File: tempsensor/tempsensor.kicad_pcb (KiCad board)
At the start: 2 copper layers, 40 x 40 mm, 36 parts, among them J1 USB_B_Micro, Q4 BSS806N, Q5 BC817, SW1 PW_OFF, SW2 PW_OFF, SW3 PW_ON, U3 24C16, U4 MCP73831-2-OT, U5 MCP9844

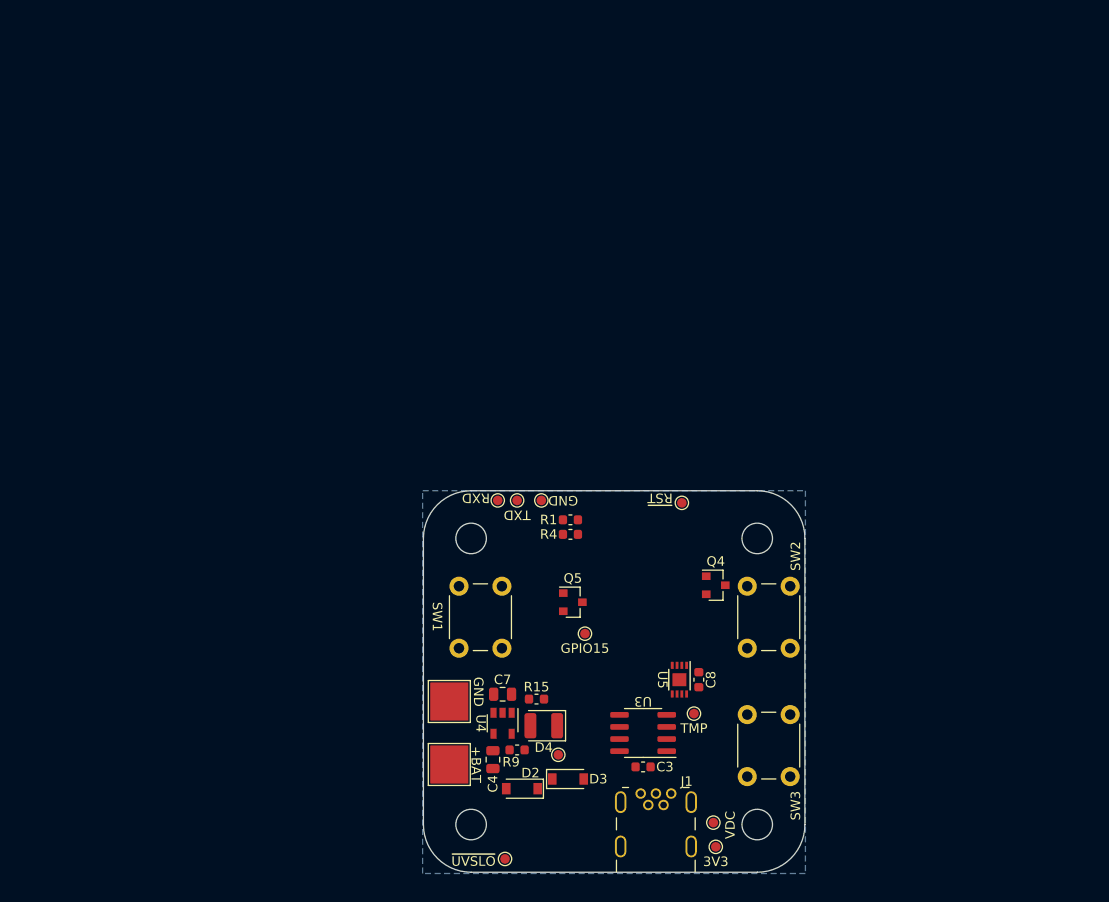
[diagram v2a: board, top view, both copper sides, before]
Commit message: Added footprints to tempsensor.
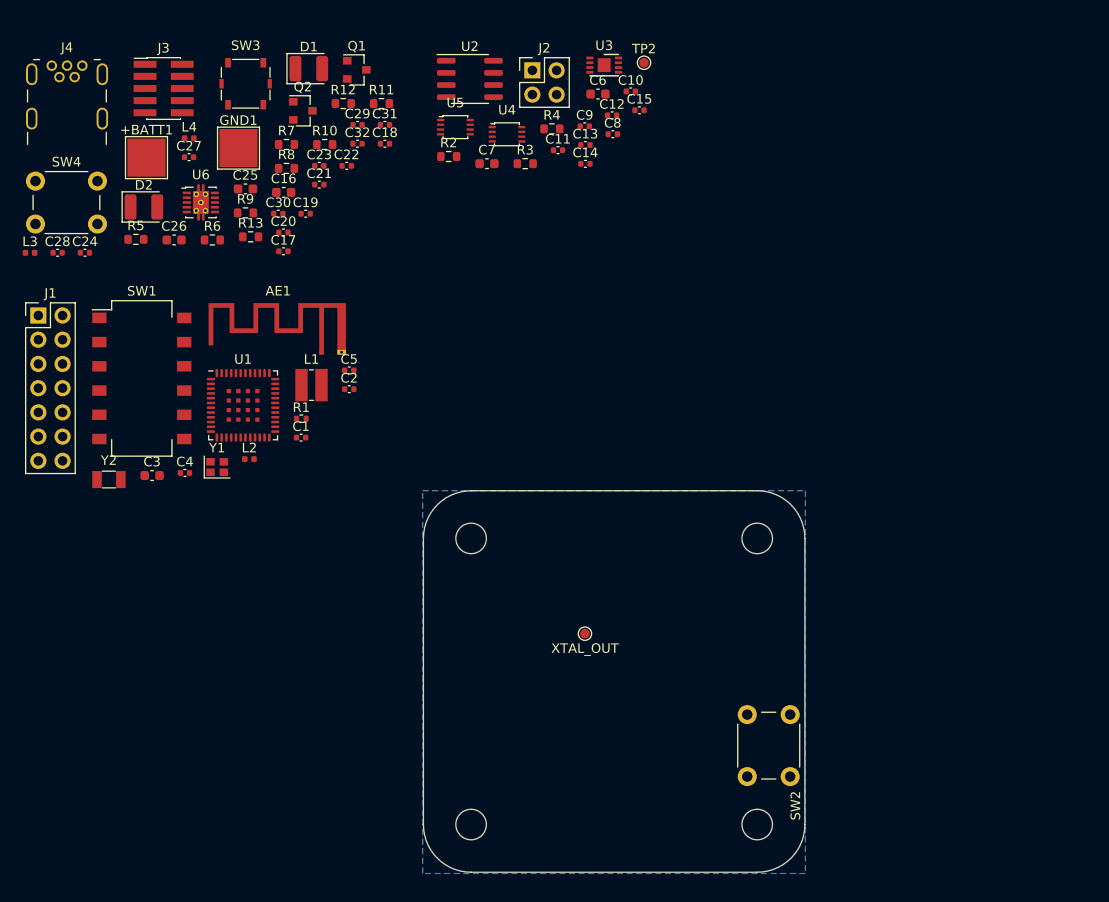
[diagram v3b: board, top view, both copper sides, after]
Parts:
- removed D3: SL03, Diode_SMD:D_SOD-123
- removed D4: LED, LED_SMD:LED_1210_3225Metric
- removed Q4: BSS806N, Package_TO_SOT_SMD:SOT-23
- removed Q5: BC817, Package_TO_SOT_SMD:SOT-23
- removed R15: 470, Resistor_SMD:R_0603_1608Metric
- removed the SW2 at (211.8, 85.1)
- removed TP12: 3V3, TestPoint:TestPoint_Pad_D1.0mm
- removed TP13: ~UVSLO, TestPoint:TestPoint_Pad_D1.0mm
- removed TP14: VDC, TestPoint:TestPoint_Pad_D1.0mm
- removed TP16: TMP, TestPoint:TestPoint_Pad_D1.0mm
- removed TP3: VBUS, TestPoint:TestPoint_Pad_D1.0mm
- removed TP4: GND, TestPoint:TestPoint_Pad_D1.0mm
- removed TP5: RXD, TestPoint:TestPoint_Pad_D1.0mm
- removed TP6: TXD, TestPoint:TestPoint_Pad_D1.0mm
- removed TP9: ~RST, TestPoint:TestPoint_Pad_D1.0mm
- added AE1: Antenna_Shield, RF_Antenna:Texas_SWRA117D_2.4GHz_Left, F.Cu at (167.2, 54.1)
- added C1: 10p, Capacitor_SMD:C_0402_1005Metric, F.Cu at (165.1, 63.0)
- added C10: 100n, Capacitor_SMD:C_0402_1005Metric, F.Cu at (199.6, 26.7)
- added C11: 1u, Capacitor_SMD:C_0402_1005Metric, F.Cu at (192.0, 32.9)
- added C12: 1u, Capacitor_SMD:C_0402_1005Metric, F.Cu at (197.7, 29.2)
- added C13: 100n, Capacitor_SMD:C_0402_1005Metric, F.Cu at (194.9, 32.3)
- added C14: 100n, Capacitor_SMD:C_0402_1005Metric, F.Cu at (194.9, 34.3)
- added C15: 1u, Capacitor_SMD:C_0402_1005Metric, F.Cu at (200.5, 28.7)
- added C16: 10u, Capacitor_SMD:C_0603_1608Metric, F.Cu at (163.2, 37.3)
- added C17: 1u, Capacitor_SMD:C_0402_1005Metric, F.Cu at (163.2, 43.5)
- added C18: 1u, Capacitor_SMD:C_0402_1005Metric, F.Cu at (173.8, 32.2)
- added C19: 100n, Capacitor_SMD:C_0402_1005Metric, F.Cu at (165.5, 39.5)
- added C2: 100n, Capacitor_SMD:C_0402_1005Metric, F.Cu at (170.1, 57.9)
- added C20: 100n, Capacitor_SMD:C_0402_1005Metric, F.Cu at (163.2, 41.5)
- added C21: 10n, Capacitor_SMD:C_0402_1005Metric, F.Cu at (167.0, 36.5)
- added C22: 10n, Capacitor_SMD:C_0402_1005Metric, F.Cu at (169.8, 34.5)
- added C23: 1u, Capacitor_SMD:C_0402_1005Metric, F.Cu at (167.0, 34.5)
- added C24: 100n, Capacitor_SMD:C_0402_1005Metric, F.Cu at (142.4, 43.6)
- added C25: 1u, Capacitor_SMD:C_0603_1608Metric, F.Cu at (159.2, 36.9)
- added C26: 10u, Capacitor_SMD:C_0603_1608Metric, F.Cu at (151.7, 42.3)
- added C27: 1u, Capacitor_SMD:C_0402_1005Metric, F.Cu at (153.3, 33.6)
- added C28: 1u, Capacitor_SMD:C_0402_1005Metric, F.Cu at (139.5, 43.6)
- added C29: 100n, Capacitor_SMD:C_0402_1005Metric, F.Cu at (171.0, 30.2)
- added C30: 12p, Capacitor_SMD:C_0402_1005Metric, F.Cu at (162.7, 39.5)
- added C31: 12p, Capacitor_SMD:C_0402_1005Metric, F.Cu at (173.8, 30.2)
- added C32: 100n, Capacitor_SMD:C_0402_1005Metric, F.Cu at (171.0, 32.2)
- added C5: 0,7p, Capacitor_SMD:C_0402_1005Metric, F.Cu at (170.1, 56.0)
- added C6: 100n, Capacitor_SMD:C_0603_1608Metric, F.Cu at (196.2, 27.0)
- added C9: 100n, Capacitor_SMD:C_0402_1005Metric, F.Cu at (194.8, 30.4)
- added D1: LED, LED_SMD:LED_1210_3225Metric, F.Cu at (165.9, 24.3)
- added J2: Conn_01x04, Connector_PinHeader_2.54mm:PinHeader_2x02_P2.54mm_Vertical, F.Cu at (189.3, 24.5)
- added J3: Conn_ARM_JTAG_SWD_10, Connector_PinHeader_1.27mm:PinHeader_2x05_P1.27mm_Vertical_SMD, F.Cu at (150.6, 26.4)
- added J4: USB_B_Micro, myfootprints:USB-Mini-B_Wuerth_651005136521_Horizontal, F.Cu at (138.9, 24.0)
- added L1: 10u, Inductor_SMD:L_Wuerth_MAPI-3012, F.Cu at (166.1, 57.5)
- added L2: 5,6n, Inductor_SMD:L_0402_1005Metric, F.Cu at (159.6, 65.3)
- added L3: 100n, Inductor_SMD:L_0402_1005Metric, F.Cu at (136.6, 43.6)
- added L4: 100n, Inductor_SMD:L_0402_1005Metric, F.Cu at (153.3, 31.6)
- added Q1: BSS806N, Package_TO_SOT_SMD:SOT-23, F.Cu at (170.9, 24.5)
- added Q2: BSS806N, Package_TO_SOT_SMD:SOT-23, F.Cu at (165.2, 28.7)
- added R10: R, Resistor_SMD:R_0603_1608Metric, F.Cu at (167.5, 32.3)
- added R11: R, Resistor_SMD:R_0603_1608Metric, F.Cu at (173.5, 28.0)
- added R12: R, Resistor_SMD:R_0603_1608Metric, F.Cu at (169.5, 28.0)
- added R13: R, Resistor_SMD:R_0603_1608Metric, F.Cu at (159.8, 42.0)
- added R2: 2K2, Resistor_SMD:R_0603_1608Metric, F.Cu at (180.5, 33.5)
- added R3: 2K2, Resistor_SMD:R_0603_1608Metric, F.Cu at (188.6, 34.3)
- added R5: R, Resistor_SMD:R_0603_1608Metric, F.Cu at (147.7, 42.2)
- added R6: R, Resistor_SMD:R_0603_1608Metric, F.Cu at (155.8, 42.3)
- added R7: R, Resistor_SMD:R_0603_1608Metric, F.Cu at (163.5, 32.3)
- added R8: R, Resistor_SMD:R_0603_1608Metric, F.Cu at (163.5, 34.8)
- added SW3: ~RST, Button_Switch_SMD:SW_SPST_Panasonic_EVQPL_3PL_5PL_PT_A08, F.Cu at (159.2, 25.9)
- added SW4: ~INT, Button_Switch_THT:SW_PUSH_6mm_H5mm, F.Cu at (137.2, 36.1)
- added TP2: ~TMP_INT, TestPoint:TestPoint_Pad_D1.0mm, F.Cu at (201.0, 23.7)
- added U1: MKW41Z512VHT, Package_DFN_QFN:NXP_LQFN-48-1EP_7x7mm_P0.5mm_EP3.5x3.5mm_16xMask0.45x0.45, F.Cu at (159.0, 59.6)
- added U2: 24C16, Package_SO:SOIC-8_3.9x4.9mm_P1.27mm, F.Cu at (182.8, 25.4)
- added U6: BQ24012, Package_SON:VSON-10-1EP_3x3mm_P0.5mm_EP1.65x2.4mm_ThermalVias, F.Cu at (154.5, 38.4)
- added Y1: 32MHz 10PPM SMT 2.0x1.6mm 10PF, Crystal:Crystal_SMD_2016-4Pin_2.0x1.6mm, F.Cu at (156.3, 66.1)
- added Y2: 32.768KHz 20PPM 3.2x1.5mm 7PF, Crystal:Crystal_SMD_3215-2Pin_3.2x1.5mm, F.Cu at (144.9, 67.4)
- C3: value 100n -> 10u
- C4: value 4u7 -> 10p; footprint Capacitor_SMD:C_0805_2012Metric -> Capacitor_SMD:C_0402_1005Metric
- C7: value 4u7 -> 10n; footprint Capacitor_SMD:C_0805_2012Metric -> Capacitor_SMD:C_0603_1608Metric
- C8: value 10n -> 1u; footprint Capacitor_SMD:C_0603_1608Metric -> Capacitor_SMD:C_0402_1005Metric
- D2: value SL03 -> LED; footprint Diode_SMD:D_SOD-123 -> LED_SMD:LED_1210_3225Metric
- J1: value USB_B_Micro -> Conn_01x14; footprint myfootprints:USB-Mini-B_Wuerth_651005136521_Horizontal -> Connector_PinHeader_2.54mm:PinHeader_2x07_P2.54mm_Vertical
- R1: value 1K -> 102K; footprint Resistor_SMD:R_0603_1608Metric -> Resistor_SMD:R_0402_1005Metric
- R4: value 1K -> R
- R9: value 2K -> R
- SW1: value PW_OFF -> SW_DIP_x06; footprint Button_Switch_THT:SW_PUSH_6mm_H5mm -> Button_Switch_SMD:SW_DIP_SPSTx06_Slide_Omron_A6S-610x_W8.9mm_P2.54mm
- TP1: value GPIO15 -> XTAL_OUT
- U3: value 24C16 -> MCP9844; footprint Package_SO:SOIC-8_3.9x4.9mm_P1.27mm -> Package_DFN_QFN:DFN-8-1EP_3x2mm_P0.5mm_EP1.36x1.46mm
- U4: value MCP73831-2-OT -> SN74LVC2T45DCUR; footprint Package_TO_SOT_SMD:SOT-23-5 -> Package_SO:VSSOP-8_2.4x2.1mm_P0.5mm
- U5: value MCP9844 -> SN74LVC2T45DCUR; footprint Package_DFN_QFN:DFN-8-1EP_3x2mm_P0.5mm_EP1.36x1.46mm -> Package_SO:VSSOP-8_2.4x2.1mm_P0.5mm
- moved J1 80.6 mm to (137.5, 50.2)
- moved D2 72.7 mm to (148.6, 38.8), turned to 0 degrees
- moved +BATT1 71.1 mm to (148.8, 33.7), turned to 0 degrees
- moved U3 70.1 mm to (196.8, 24.0), turned to 0 degrees
- moved R9 63.1 mm to (159.2, 39.4)
- moved U5 62.5 mm to (181.2, 30.5), turned to 0 degrees
- moved GND1 62.1 mm to (158.5, 32.7), turned to 0 degrees
- moved U4 61.8 mm to (186.6, 31.2), turned to 0 degrees
- moved C3 59.9 mm to (149.4, 67.0)
- moved C8 57.9 mm to (197.7, 31.2), turned to 0 degrees
- moved C7 55.7 mm to (184.5, 34.3), turned to 0 degrees
- moved C4 44.1 mm to (152.9, 66.7), turned to 0 degrees
- moved SW1 43.7 mm to (148.4, 56.8), turned to 0 degrees
- moved R4 42.6 mm to (191.4, 30.6), turned to 0 degrees
- moved R1 30.1 mm to (165.1, 61.0), turned to 0 degrees
- renumbered SW3 to SW2
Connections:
- C3 pad 1: +3V3 -> +BATT
- C4 pad 1: VBUS -> Net-(AE1-Pad1)
- C4 pad 2: GND -> Net-(C4-Pad2)
- C7 pad 1: GND -> +1V8
- C7 pad 2: +BATT -> GND
- C8 pad 1: +3V3 -> +1V8
- D2 pad 1: +VDC -> Net-(D2-Pad1)
- D2 pad 2: +BATT -> Net-(D2-Pad2)
- J1 pad 1: VBUS -> +1V8
- J1 pad 2: (no net) -> +BATT
- J1 pad 3: (no net) -> /PTC1
- J1 pad 4: (no net) -> /PTC4
- J1 pad 5: GND -> /PTC19
- J1 pad 6: GND -> /~BTN_INT
- R1 pad 1: +3V3 -> Net-(C2-Pad1)
- R1 pad 2: /SCL -> GND
- R4 pad 1: +3V3 -> /~TMP_INT
- R4 pad 2: /SDA -> +1V8
- R9 pad 1: Net-(R9-Pad1) -> Net-(D1-Pad2)
- R9 pad 2: GND -> VBUS
- SW1 pad 1: Net-(SW1-Pad1) -> /PTB2
- SW1 pad 2: Net-(SW1-Pad2) -> /PTB3
- SW2 pad 1: Net-(SW3-Pad1) -> Net-(C2-Pad1)
- SW2 pad 2: Net-(SW3-Pad2) -> +BATT
- TP1 pad 1: (no net) -> /XTAL_OUT
- U3 pad 7: GND -> /~TMP_INT
- U3 pad 8: +3V3 -> +1V8
- U4 pad 1: Net-(R15-Pad2) -> +1V8
- U4 pad 2: GND -> /LPUART0_TX
- U4 pad 3: +BATT -> GND
- U4 pad 4: VBUS -> GND
- U4 pad 5: Net-(R9-Pad1) -> +1V8
- U5 pad 1: GND -> +1V8
- U5 pad 2: GND -> /LPUART0_RX
- U5 pad 3: GND -> Net-(U5-Pad3)
- U5 pad 5: /SDA -> GND
- U5 pad 6: /SCL -> GND
- U5 pad 7: (no net) -> /I2C/UART_RX
- U5 pad 8: +3V3 -> +VDC

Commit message: Started layouting the TempSensor, exchanged the large LEDs for 0603 LEDs (from ELAB). MCU needs to be placed. Changed signals on expansion header to put power pins onto just one end.
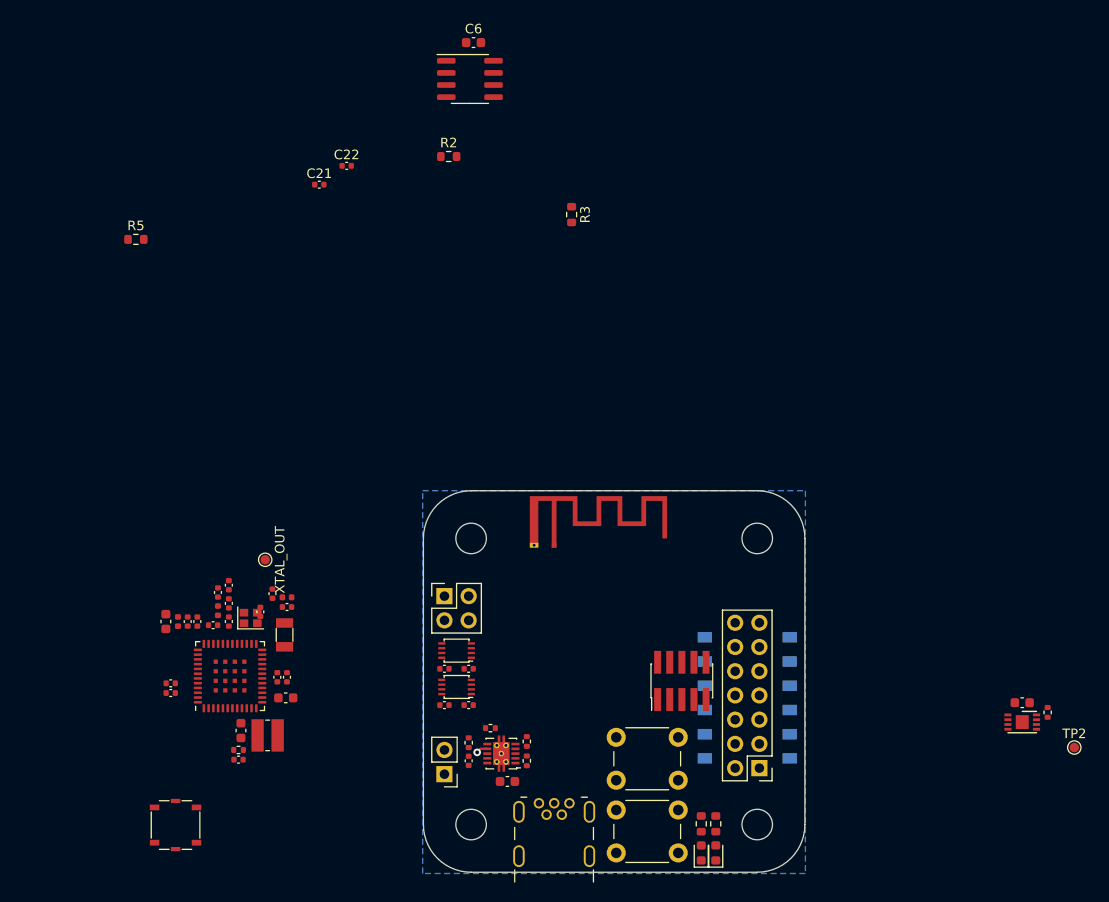
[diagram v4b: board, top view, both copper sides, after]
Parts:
- removed +BATT1: +BAT, TestPoint:TestPoint_Pad_4.0x4.0mm
- removed C11, C12, C15, C8: 1u, Capacitor_SMD:C_0402_1005Metric
- removed GND1: GND, TestPoint:TestPoint_Pad_4.0x4.0mm
- removed Q1, Q2: BSS806N, Package_TO_SOT_SMD:SOT-23
- removed R10, R9: R, Resistor_SMD:R_0603_1608Metric
- added J5: Conn_01x02, Connector_PinHeader_2.54mm:PinHeader_1x02_P2.54mm_Vertical, F.Cu at (180.1, 98.3)
- AE1: footprint RF_Antenna:Texas_SWRA117D_2.4GHz_Left -> RF_Antenna:Texas_SWRA117D_2.4GHz_Right
- D1, D2: footprint LED_SMD:LED_1210_3225Metric -> LED_SMD:LED_0603_1608Metric
- R11, R4, R6, R7, R8: footprint Resistor_SMD:R_0603_1608Metric -> Resistor_SMD:R_0402_1005Metric
- SW1: moved to B.Cu
- moved J4 92.7 mm to (190.0, 101.3)
- moved SW4 92.1 mm to (204.6, 98.9), turned to 180 degrees
- moved D1 91.9 mm to (207.0, 106.6), turned to 90 degrees
- moved D2 90.5 mm to (208.5, 106.6), turned to 90 degrees
- moved J1 89.3 mm to (213.1, 97.7), turned to 180 degrees
- moved TP2 84.8 mm to (246.1, 95.5)
- moved R12 84.3 mm to (207.0, 103.5), turned to 90 degrees
- moved J3 82.5 mm to (205.0, 88.5), turned to 90 degrees
- moved U3 81.6 mm to (240.7, 92.8)
- moved R4 80.3 mm to (243.3, 91.8), turned to 90 degrees
- moved C7 79.6 mm to (240.7, 90.8), turned to 180 degrees
- moved R13 78.5 mm to (208.5, 103.5), turned to 90 degrees
- moved SW3 78.1 mm to (151.9, 103.6), turned to 270 degrees
- moved SW1 71.8 mm to (211.8, 90.3)
- moved C25 67.9 mm to (186.7, 99.1)
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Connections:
- D1 pad 1: Net-(D1-Pad1) -> GND
- D2 pad 1: Net-(D2-Pad1) -> GND
- J1 pad 10: /TMP0_CH3 -> /PTB3
- J1 pad 11: /PTA16 -> /TMP0_CH2
- J1 pad 12: /PTA17 -> /TMP0_CH3
- J1 pad 13: GND -> /PTA16
- J1 pad 14: GND -> /PTA17
- J1 pad 3: /PTC1 -> GND
- J1 pad 4: /PTC4 -> GND
- J1 pad 5: /PTC19 -> /PTC1
- J1 pad 6: /~BTN_INT -> /PTC4
- J1 pad 7: /PTB2 -> /PTC19
- J1 pad 8: /PTB3 -> /~BTN_INT
- J1 pad 9: /TMP0_CH2 -> /PTB2
- R12 pad 1: Net-(Q1-Pad1) -> Net-(D1-Pad2)
- R13 pad 1: Net-(Q2-Pad1) -> Net-(D2-Pad2)
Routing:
- net /~CHG_PG: track 0.00 -> 1.22 mm, vias 0 -> 1

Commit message: Continued routing of tempsensor, basic functionality done.
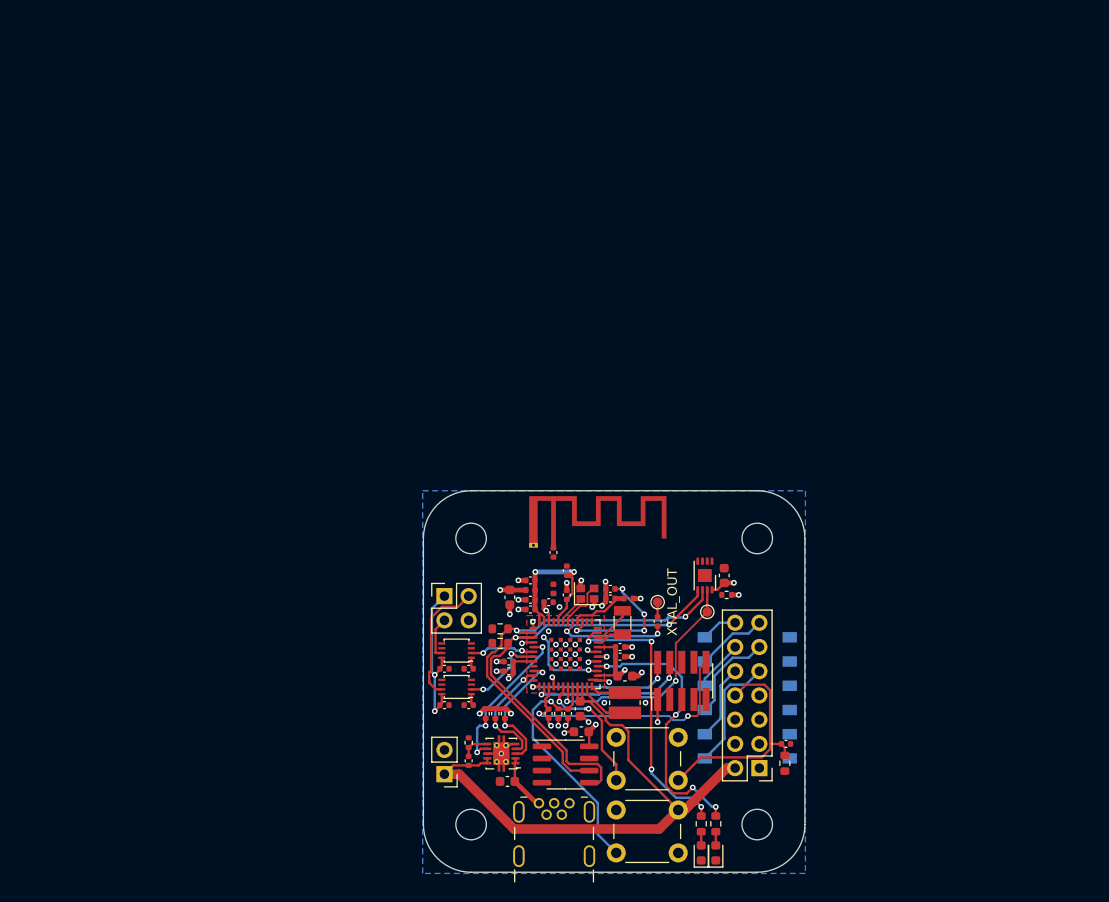
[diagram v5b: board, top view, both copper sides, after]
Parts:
- removed SW3: ~RST, Button_Switch_SMD:SW_SPST_Panasonic_EVQPL_3PL_5PL_PT_A08
- moved R5 87.4 mm to (215.8, 97.2), turned to 270 degrees
- moved C22 76.1 mm to (215.9, 95.1)
- moved C6 73.1 mm to (194.4, 93.9), turned to 180 degrees
- moved U2 72.6 mm to (192.8, 97.3)
- moved C21 60.5 mm to (191.0, 91.9), turned to 270 degrees
- moved R2 49.8 mm to (185.9, 83.1)
- moved R3 45.6 mm to (185.9, 84.6), turned to 0 degrees
- moved C1 41.7 mm to (202.4, 82.3)
- moved TP1 41.4 mm to (202.4, 80.3)
- moved TP2 41.0 mm to (207.6, 81.3)
- moved L1 37.6 mm to (199.0, 90.8), turned to 270 degrees
- moved L4 37.1 mm to (189.1, 79.0), turned to 0 degrees
- moved U3 36.7 mm to (207.4, 77.5), turned to 270 degrees
- moved C26 36.2 mm to (186.9, 79.8), turned to 270 degrees
- moved C20 36.1 mm to (198.5, 85.0), turned to 0 degrees
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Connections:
- C22 pad 1: /MKW41_PERIPHERAL_PWR/~BTN_INT -> /~BTN_INT
- R5 pad 1: /MKW41_PERIPHERAL_PWR/~BTN_INT -> /~BTN_INT
- SW4 pad 1: /MKW41_PERIPHERAL_PWR/~BTN_INT -> /~BTN_INT
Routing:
- net +BATT: track 0.00 -> 61.3 mm
- net /SDA: track 0.00 -> 47.8 mm, vias 0 -> 2
- net /SCL: track 0.00 -> 46.2 mm, vias 0 -> 2
- net /~BTN_INT: track 0.00 -> 38.0 mm, vias 0 -> 2
- net /TMP0_CH0: track 0.00 -> 29.8 mm, vias 0 -> 4
- net /TMP0_CH1: track 0.00 -> 29.2 mm, vias 0 -> 4
- net +1V8: track 0.00 -> 27.6 mm, vias 0 -> 9
- net /~MCU_RST: track 0.00 -> 26.8 mm, vias 0 -> 2
- net GND: track 0.00 -> 25.7 mm, vias 0 -> 34
- net /~TMP_INT: track 0.00 -> 25.6 mm, vias 0 -> 2
- net Net-(C2-Pad1): track 0.00 -> 25.6 mm, vias 0 -> 1
- net +1V5: track 0.00 -> 19.3 mm, vias 0 -> 3
- net /VDD_RF: track 0.00 -> 17.5 mm, vias 0 -> 2
- net +VDC: track 0.00 -> 16.9 mm, vias 0 -> 2
- net /SWD_CLK: track 0.00 -> 16.8 mm, vias 0 -> 2
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- added copper zone on In2.Cu, net +1V8
- added copper zone on F.Cu, net GND
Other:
- copper layers 2 -> 4
- net class Default: clearance 0.2 -> 0.15; trace_width 0.25 -> 0.15; via_dia 0.8 -> 0.6; via_drill 0.4 -> 0.3
- rule trace_clearance: 0.2 -> 0.15
- rule trace_min: 0.2 -> 0.15
